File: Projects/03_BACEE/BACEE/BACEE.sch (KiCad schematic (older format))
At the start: 12 parts

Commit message: Project 3: Arrange symbols
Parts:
- added U?: 24LC1025, symbol Memory_EEPROM:24LC1025
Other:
- moved on the sheet: BT?, C?, D?, R?, U?, Y?
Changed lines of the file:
@@
 L Device:Battery BT?
 U 1 1 61D22E5D
-P 5250 2650
-F 0 "BT?" H 5358 2696 50  0000 L CNN
-F 1 "Battery" H 5358 2605 50  0000 L CNN
-F 2 "" V 5250 2710 50  0001 C CNN
-F 3 "~" V 5250 2710 50  0001 C CNN
-	1    5250 2650
+P 9250 2100
+F 0 "BT?" H 9358 2146 50  0000 L CNN
+F 1 "Battery" H 9358 2055 50  0000 L CNN
+F 2 "" V 9250 2160 50  0001 C CNN
+F 3 "~" V 9250 2160 50  0001 C CNN
+	1    9250 2100
 	1    0    0    -1
 $EndComp
@@
 L Device:LED D?
 U 1 1 61D23F53
-P 5250 3200
-F 0 "D?" H 5243 3417 50  0000 C CNN
-F 1 "LED" H 5243 3326 50  0000 C CNN
-F 2 "" H 5250 3200 50  0001 C CNN
-F 3 "~" H 5250 3200 50  0001 C CNN
-	1    5250 3200
+P 5600 3150
+F 0 "D?" H 5593 3367 50  0000 C CNN
+F 1 "LED" H 5593 3276 50  0000 C CNN
+F 2 "" H 5600 3150 50  0001 C CNN
+F 3 "~" H 5600 3150 50  0001 C CNN
+	1    5600 3150
 	1    0    0    -1
 $EndComp
@@
 L Device:C C?
 U 1 1 61D244B0
-P 6100 2350
-F 0 "C?" H 6215 2396 50  0000 L CNN
-F 1 "C" H 6215 2305 50  0000 L CNN
-F 2 "" H 6138 2200 50  0001 C CNN
-F 3 "~" H 6100 2350 50  0001 C CNN
-	1    6100 2350
+P 5050 2050
+F 0 "C?" H 5165 2096 50  0000 L CNN
+F 1 "C" H 5165 2005 50  0000 L CNN
+F 2 "" H 5088 1900 50  0001 C CNN
+F 3 "~" H 5050 2050 50  0001 C CNN
+	1    5050 2050
 	1    0    0    -1
 $EndComp
@@
 L Device:C C?
 U 1 1 61D24B04
-P 6100 2900
-F 0 "C?" H 6215 2946 50  0000 L CNN
-F 1 "C" H 6215 2855 50  0000 L CNN
-F 2 "" H 6138 2750 50  0001 C CNN
-F 3 "~" H 6100 2900 50  0001 C CNN
-	1    6100 2900
+P 5050 2600
+F 0 "C?" H 5165 2646 50  0000 L CNN
+F 1 "C" H 5165 2555 50  0000 L CNN
+F 2 "" H 5088 2450 50  0001 C CNN
+F 3 "~" H 5050 2600 50  0001 C CNN
+	1    5050 2600
 	1    0    0    -1
 $EndComp
@@
 L Device:CP C?
 U 1 1 61D25462
-P 6100 3450
-F 0 "C?" H 6218 3496 50  0000 L CNN
-F 1 "CP" H 6218 3405 50  0000 L CNN
-F 2 "" H 6138 3300 50  0001 C CNN
-F 3 "~" H 6100 3450 50  0001 C CNN
-	1    6100 3450
+P 9950 2750
+F 0 "C?" H 10068 2796 50  0000 L CNN
+F 1 "CP" H 10068 2705 50  0000 L CNN
+F 2 "" H 9988 2600 50  0001 C CNN
+F 3 "~" H 9950 2750 50  0001 C CNN
+	1    9950 2750
 	1    0    0    -1
 $EndComp
@@
 L Device:R R?
 U 1 1 61D25BF7
-P 6900 2350
-F 0 "R?" H 6970 2396 50  0000 L CNN
-F 1 "R" H 6970 2305 50  0000 L CNN
-F 2 "" V 6830 2350 50  0001 C CNN
-F 3 "~" H 6900 2350 50  0001 C CNN
-	1    6900 2350
+P 4950 3300
+F 0 "R?" H 5020 3346 50  0000 L CNN
+F 1 "R" H 5020 3255 50  0000 L CNN
+F 2 "" V 4880 3300 50  0001 C CNN
+F 3 "~" H 4950 3300 50  0001 C CNN
+	1    4950 3300
 	1    0    0    -1
 $EndComp
@@
 L Device:R R?
 U 1 1 61D26130
-P 6900 2900
-F 0 "R?" H 6970 2946 50  0000 L CNN
-F 1 "R" H 6970 2855 50  0000 L CNN
-F 2 "" V 6830 2900 50  0001 C CNN
-F 3 "~" H 6900 2900 50  0001 C CNN
-	1    6900 2900
+P 4950 3850
+F 0 "R?" H 5020 3896 50  0000 L CNN
+F 1 "R" H 5020 3805 50  0000 L CNN
+F 2 "" V 4880 3850 50  0001 C CNN
+F 3 "~" H 4950 3850 50  0001 C CNN
+	1    4950 3850
 	1    0    0    -1
 $EndComp
@@
 L Memory_EEPROM:24LC1025 U?
 U 1 1 61D26D32
-P 8000 2600
-F 0 "U?" H 8000 3081 50  0000 C CNN
-F 1 "24LC1025" H 8000 2990 50  0000 C CNN
-F 2 "" H 8000 2600 50  0001 C CNN
-F 3 "http://ww1.microchip.com/downloads/en/DeviceDoc/21941B.pdf" H 8000 2600 50  0001 C CNN
-	1    8000 2600
+P 3000 5100
+F 0 "U?" H 3000 5581 50  0000 C CNN
+F 1 "24LC1025" H 3000 5490 50  0000 C CNN
+F 2 "" H 3000 5100 50  0001 C CNN
+F 3 "http://ww1.microchip.com/downloads/en/DeviceDoc/21941B.pdf" H 3000 5100 50  0001 C CNN
+	1    3000 5100
 	1    0    0    -1
 $EndComp
 $Sheet
-S 7600 3250 1650 2150
+S 5100 5900 1000 1100
 U 61D27AD2
 F0 "Connectors" 50
@@
 L MCU_Microchip_ATmega:ATmega328P-AU U?
 U 1 1 61D2E20A
-P 4150 3750
-F 0 "U?" H 4150 2161 50  0000 C CNN
-F 1 "ATmega328P-AU" H 4150 2070 50  0000 C CNN
-F 2 "Package_QFP:TQFP-32_7x7mm_P0.8mm" H 4150 3750 50  0001 C CIN
-F 3 "http://ww1.microchip.com/downloads/en/DeviceDoc/ATmega328_P%20AVR%20MCU%20with%20picoPower%20Technology%20Data%20Sheet%2040001984A.pdf" H 4150 3750 50  0001 C CNN
-	1    4150 3750
+P 7000 3500
+F 0 "U?" H 7000 1911 50  0000 C CNN
+F 1 "ATmega328P-AU" H 7000 1820 50  0000 C CNN
+F 2 "Package_QFP:TQFP-32_7x7mm_P0.8mm" H 7000 3500 50  0001 C CIN
+F 3 "http://ww1.microchip.com/downloads/en/DeviceDoc/ATmega328_P%20AVR%20MCU%20with%20picoPower%20Technology%20Data%20Sheet%2040001984A.pdf" H 7000 3500 50  0001 C CNN
+	1    7000 3500
 	1    0    0    -1
 $EndComp
@@
 L Project3:DS1337_MLv1 U?
 U 1 1 61D31649
-P 6200 4800
-F 0 "U?" H 6200 5031 50  0000 C CNN
-F 1 "DS1337_MLv1" H 6200 4940 50  0000 C CNN
-F 2 "" H 6500 4800 50  0001 C CNN
-F 3 "https://datasheets.maximintegrated.com/en/ds/DS1337-DS1337C.pdf" H 6500 4800 50  0001 C CNN
-	1    6200 4800
+P 2950 2150
+F 0 "U?" H 2950 2381 50  0000 C CNN
+F 1 "DS1337_MLv1" H 2950 2290 50  0000 C CNN
+F 2 "" H 3250 2150 50  0001 C CNN
+F 3 "https://datasheets.maximintegrated.com/en/ds/DS1337-DS1337C.pdf" H 3250 2150 50  0001 C CNN
+	1    2950 2150
 	1    0    0    -1
 $EndComp
@@
 L Device:Crystal Y?
 U 1 1 61D3267A
-P 2950 2550
-F 0 "Y?" H 2950 2818 50  0000 C CNN
-F 1 "Crystal" H 2950 2727 50  0000 C CNN
-F 2 "" H 2950 2550 50  0001 C CNN
-F 3 "~" H 2950 2550 50  0001 C CNN
-	1    2950 2550
-	1    0    0    -1
+P 5800 2300
+F 0 "Y?" V 5754 2431 50  0000 L CNN
+F 1 "Crystal" V 5845 2431 50  0000 L CNN
+F 2 "" H 5800 2300 50  0001 C CNN
+F 3 "~" H 5800 2300 50  0001 C CNN
+	1    5800 2300
+	0    1    1    0
 $EndComp
 $Comp
 L Device:Crystal Y?
 U 1 1 61D331D7
-P 2950 3350
-F 0 "Y?" H 2950 3618 50  0000 C CNN
-F 1 "Crystal" H 2950 3527 50  0000 C CNN
-F 2 "" H 2950 3350 50  0001 C CNN
-F 3 "~" H 2950 3350 50  0001 C CNN
-	1    2950 3350
+P 1900 2450
+F 0 "Y?" H 1900 2718 50  0000 C CNN
+F 1 "Crystal" H 1900 2627 50  0000 C CNN
+F 2 "" H 1900 2450 50  0001 C CNN
+F 3 "~" H 1900 2450 50  0001 C CNN
+	1    1900 2450
 	1    0    0    -1
 $EndComp
+$Comp
+L Memory_EEPROM:24LC1025 U?
+U 1 1 61D3DE19
+P 3000 4100
+F 0 "U?" H 3000 4581 50  0000 C CNN
+F 1 "24LC1025" H 3000 4490 50  0000 C CNN
+F 2 "" H 3000 4100 50  0001 C CNN
+F 3 "http://ww1.microchip.com/downloads/en/DeviceDoc/21941B.pdf" H 3000 4100 50  0001 C CNN
+	1    3000 4100
+	1    0    0    -1
+$EndComp
+$Comp
+L power:GND #PWR?
+U 1 1 61D47A07
+P 9250 3300
+F 0 "#PWR?" H 9250 3050 50  0001 C CNN
+F 1 "GND" H 9255 3127 50  0000 C CNN
+F 2 "" H 9250 3300 50  0001 C CNN
+F 3 "" H 9250 3300 50  0001 C CNN
+	1    9250 3300
+	1    0    0    -1
+$EndComp

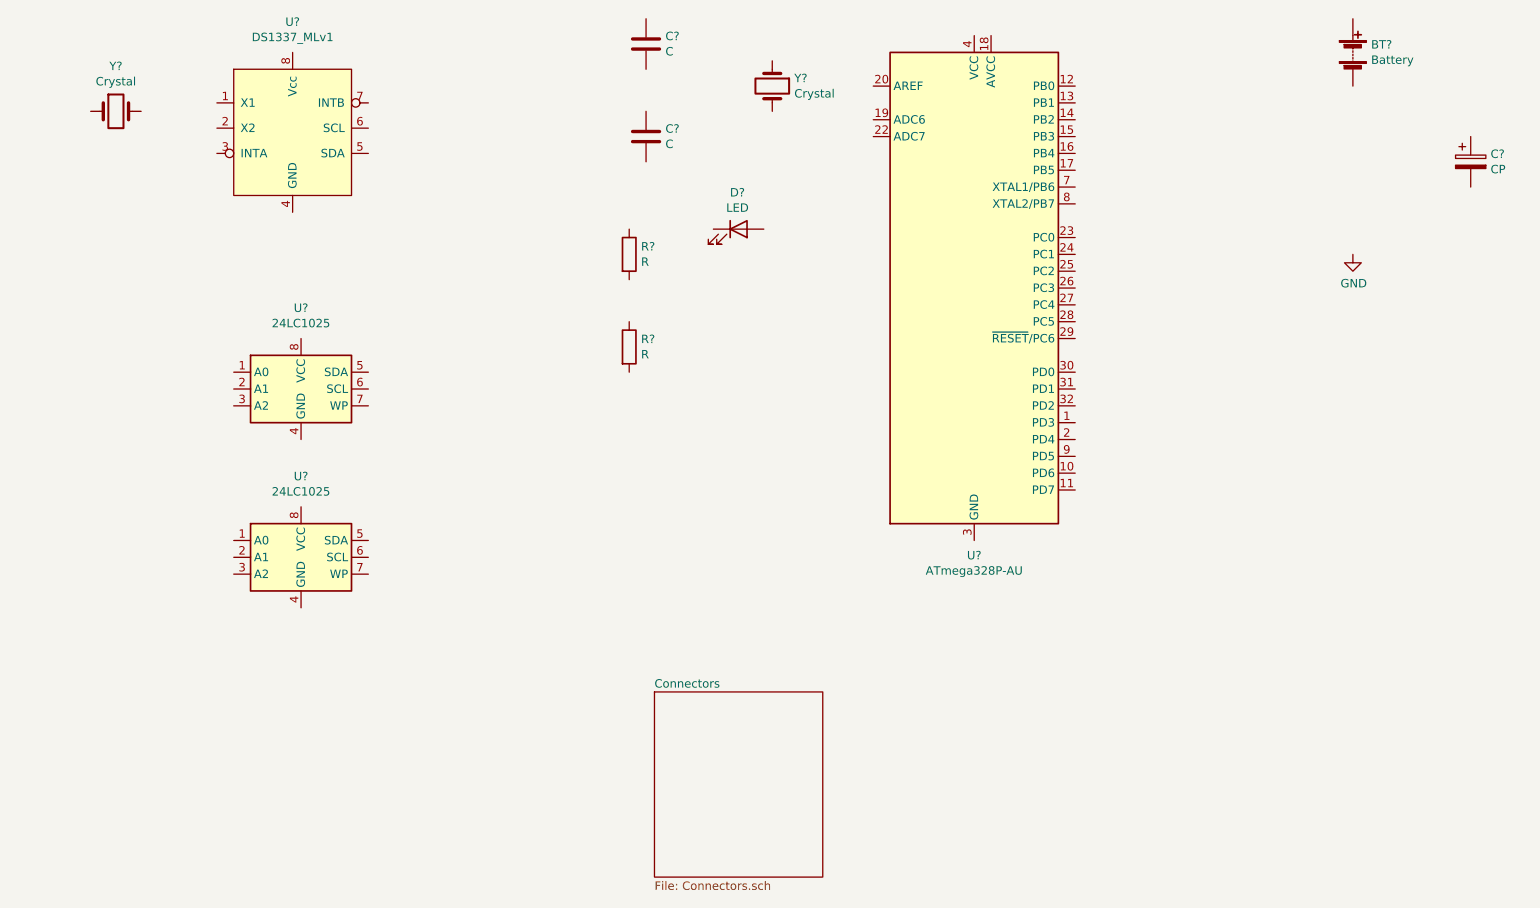
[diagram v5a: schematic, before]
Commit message: Project 3: Annotate schematic
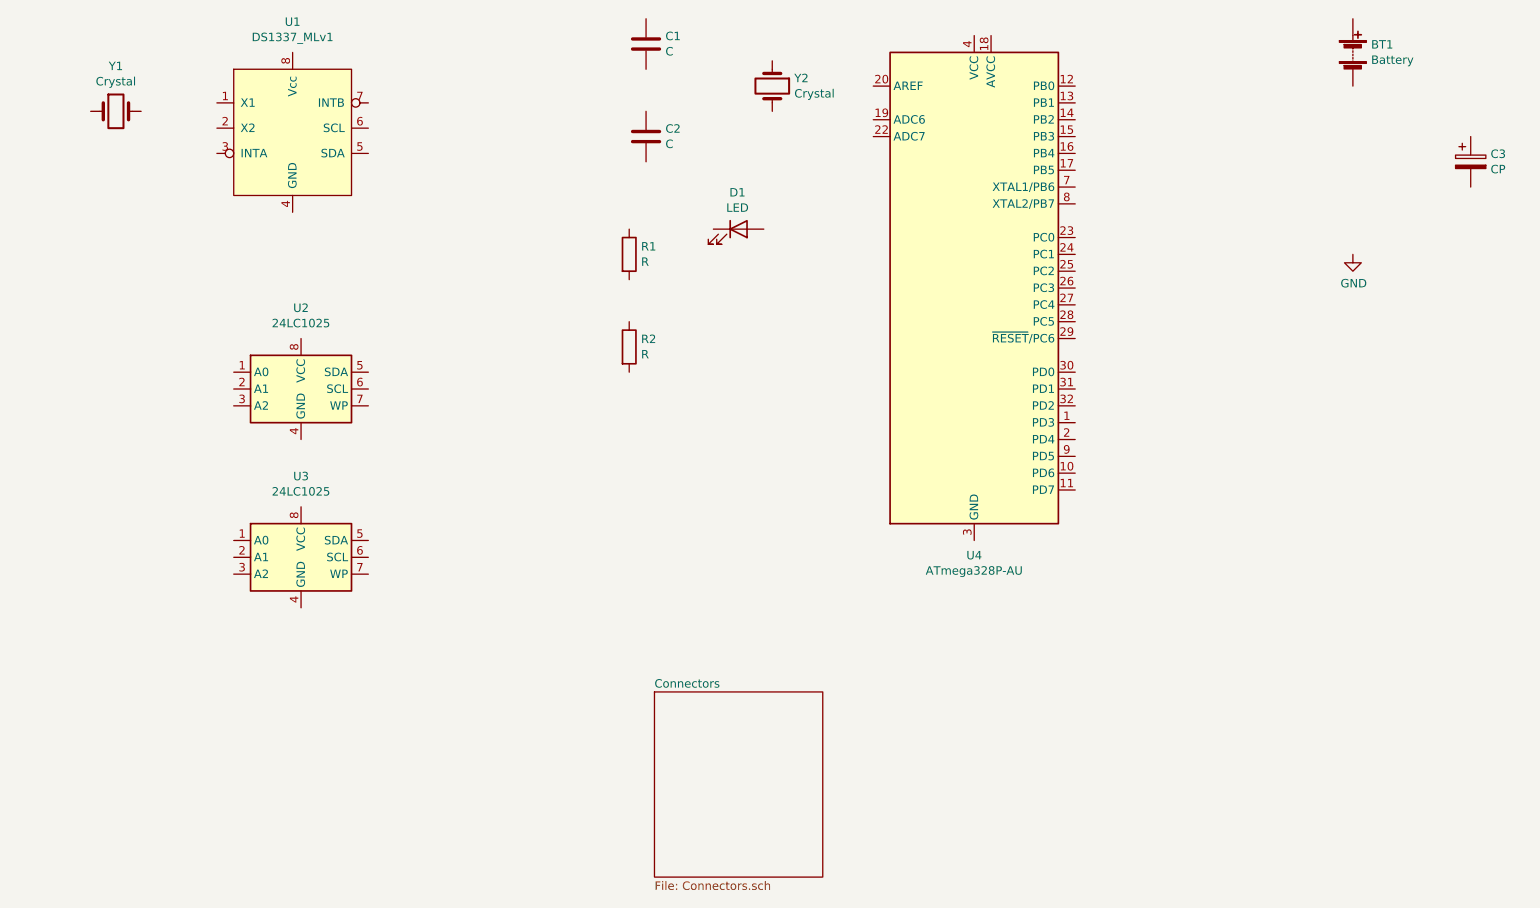
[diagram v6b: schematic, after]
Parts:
- gave numbers to parts that had none: 13
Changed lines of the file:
@@
 $EndDescr
 $Comp
-L Device:Battery BT?
+L Device:Battery BT1
 U 1 1 61D22E5D
 P 9250 2100
-F 0 "BT?" H 9358 2146 50  0000 L CNN
+F 0 "BT1" H 9358 2146 50  0000 L CNN
 F 1 "Battery" H 9358 2055 50  0000 L CNN
 F 2 "" V 9250 2160 50  0001 C CNN
@@
 $EndComp
 $Comp
-L Device:LED D?
+L Device:LED D1
 U 1 1 61D23F53
 P 5600 3150
-F 0 "D?" H 5593 3367 50  0000 C CNN
+F 0 "D1" H 5593 3367 50  0000 C CNN
 F 1 "LED" H 5593 3276 50  0000 C CNN
 F 2 "" H 5600 3150 50  0001 C CNN
@@
 $EndComp
 $Comp
-L Device:C C?
+L Device:C C1
 U 1 1 61D244B0
 P 5050 2050
-F 0 "C?" H 5165 2096 50  0000 L CNN
+F 0 "C1" H 5165 2096 50  0000 L CNN
 F 1 "C" H 5165 2005 50  0000 L CNN
 F 2 "" H 5088 1900 50  0001 C CNN
@@
 $EndComp
 $Comp
-L Device:C C?
+L Device:C C2
 U 1 1 61D24B04
 P 5050 2600
-F 0 "C?" H 5165 2646 50  0000 L CNN
+F 0 "C2" H 5165 2646 50  0000 L CNN
 F 1 "C" H 5165 2555 50  0000 L CNN
 F 2 "" H 5088 2450 50  0001 C CNN
@@
 $EndComp
 $Comp
-L Device:CP C?
+L Device:CP C3
 U 1 1 61D25462
 P 9950 2750
-F 0 "C?" H 10068 2796 50  0000 L CNN
+F 0 "C3" H 10068 2796 50  0000 L CNN
 F 1 "CP" H 10068 2705 50  0000 L CNN
 F 2 "" H 9988 2600 50  0001 C CNN
@@
 $EndComp
 $Comp
-L Device:R R?
+L Device:R R1
 U 1 1 61D25BF7
 P 4950 3300
-F 0 "R?" H 5020 3346 50  0000 L CNN
+F 0 "R1" H 5020 3346 50  0000 L CNN
 F 1 "R" H 5020 3255 50  0000 L CNN
 F 2 "" V 4880 3300 50  0001 C CNN
@@
 $EndComp
 $Comp
-L Device:R R?
+L Device:R R2
 U 1 1 61D26130
 P 4950 3850
-F 0 "R?" H 5020 3896 50  0000 L CNN
+F 0 "R2" H 5020 3896 50  0000 L CNN
 F 1 "R" H 5020 3805 50  0000 L CNN
 F 2 "" V 4880 3850 50  0001 C CNN
@@
 $EndComp
 $Comp
-L Memory_EEPROM:24LC1025 U?
+L Memory_EEPROM:24LC1025 U3
 U 1 1 61D26D32
 P 3000 5100
-F 0 "U?" H 3000 5581 50  0000 C CNN
+F 0 "U3" H 3000 5581 50  0000 C CNN
 F 1 "24LC1025" H 3000 5490 50  0000 C CNN
 F 2 "" H 3000 5100 50  0001 C CNN
@@
 $EndSheet
 $Comp
-L MCU_Microchip_ATmega:ATmega328P-AU U?
+L MCU_Microchip_ATmega:ATmega328P-AU U4
 U 1 1 61D2E20A
 P 7000 3500
-F 0 "U?" H 7000 1911 50  0000 C CNN
+F 0 "U4" H 7000 1911 50  0000 C CNN
 F 1 "ATmega328P-AU" H 7000 1820 50  0000 C CNN
 F 2 "Package_QFP:TQFP-32_7x7mm_P0.8mm" H 7000 3500 50  0001 C CIN
@@
 $EndComp
 $Comp
-L Project3:DS1337_MLv1 U?
+L Project3:DS1337_MLv1 U1
 U 1 1 61D31649
 P 2950 2150
-F 0 "U?" H 2950 2381 50  0000 C CNN
+F 0 "U1" H 2950 2381 50  0000 C CNN
 F 1 "DS1337_MLv1" H 2950 2290 50  0000 C CNN
 F 2 "" H 3250 2150 50  0001 C CNN
@@
 $EndComp
 $Comp
-L Device:Crystal Y?
+L Device:Crystal Y2
 U 1 1 61D3267A
 P 5800 2300
-F 0 "Y?" V 5754 2431 50  0000 L CNN
+F 0 "Y2" V 5754 2431 50  0000 L CNN
 F 1 "Crystal" V 5845 2431 50  0000 L CNN
 F 2 "" H 5800 2300 50  0001 C CNN
@@
 $EndComp
 $Comp
-L Device:Crystal Y?
+L Device:Crystal Y1
 U 1 1 61D331D7
 P 1900 2450
-F 0 "Y?" H 1900 2718 50  0000 C CNN
+F 0 "Y1" H 1900 2718 50  0000 C CNN
 F 1 "Crystal" H 1900 2627 50  0000 C CNN
 F 2 "" H 1900 2450 50  0001 C CNN
@@
 $EndComp
 $Comp
-L Memory_EEPROM:24LC1025 U?
+L Memory_EEPROM:24LC1025 U2
 U 1 1 61D3DE19
 P 3000 4100
-F 0 "U?" H 3000 4581 50  0000 C CNN
+F 0 "U2" H 3000 4581 50  0000 C CNN
 F 1 "24LC1025" H 3000 4490 50  0000 C CNN
 F 2 "" H 3000 4100 50  0001 C CNN
@@
 $EndComp
 $Comp
-L power:GND #PWR?
+L power:GND #PWR01
 U 1 1 61D47A07
 P 9250 3300
-F 0 "#PWR?" H 9250 3050 50  0001 C CNN
+F 0 "#PWR01" H 9250 3050 50  0001 C CNN
 F 1 "GND" H 9255 3127 50  0000 C CNN
 F 2 "" H 9250 3300 50  0001 C CNN

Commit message: Project 3: Associate footprints
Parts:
- BT1: footprint (none) -> Connector_PinHeader_2.54mm:PinHeader_1x02_P2.54mm_Vertical
- C1, C2, C3: footprint (none) -> Diode_SMD:D_0805_2012Metric_Pad1.15x1.40mm_HandSolder
- D1: footprint (none) -> LED_SMD:LED_0805_2012Metric_Pad1.15x1.40mm_HandSolder
- R1, R2: footprint (none) -> Resistor_SMD:R_0805_2012Metric_Pad1.20x1.40mm_HandSolder
- U1: footprint (none) -> Package_SO:SO-8_5.3x6.2mm_P1.27mm
- U2, U3: footprint (none) -> Package_SO:SOIJ-8_5.3x5.3mm_P1.27mm
- Y1: footprint (none) -> Crystal:Crystal_SMD_MicroCrystal_CC7V-T1A-2Pin_3.2x1.5mm
- Y2: footprint (none) -> Crystal:Crystal_SMD_5032-2Pin_5.0x3.2mm_HandSoldering
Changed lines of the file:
@@
 F 0 "BT1" H 9358 2146 50  0000 L CNN
 F 1 "Battery" H 9358 2055 50  0000 L CNN
-F 2 "" V 9250 2160 50  0001 C CNN
+F 2 "Connector_PinHeader_2.54mm:PinHeader_1x02_P2.54mm_Vertical" V 9250 2160 50  0001 C CNN
 F 3 "~" V 9250 2160 50  0001 C CNN
 	1    9250 2100
@@
 F 0 "D1" H 5593 3367 50  0000 C CNN
 F 1 "LED" H 5593 3276 50  0000 C CNN
-F 2 "" H 5600 3150 50  0001 C CNN
+F 2 "LED_SMD:LED_0805_2012Metric_Pad1.15x1.40mm_HandSolder" H 5600 3150 50  0001 C CNN
 F 3 "~" H 5600 3150 50  0001 C CNN
 	1    5600 3150
@@
 F 0 "C1" H 5165 2096 50  0000 L CNN
 F 1 "C" H 5165 2005 50  0000 L CNN
-F 2 "" H 5088 1900 50  0001 C CNN
+F 2 "Diode_SMD:D_0805_2012Metric_Pad1.15x1.40mm_HandSolder" H 5088 1900 50  0001 C CNN
 F 3 "~" H 5050 2050 50  0001 C CNN
 	1    5050 2050
@@
 F 0 "C2" H 5165 2646 50  0000 L CNN
 F 1 "C" H 5165 2555 50  0000 L CNN
-F 2 "" H 5088 2450 50  0001 C CNN
+F 2 "Diode_SMD:D_0805_2012Metric_Pad1.15x1.40mm_HandSolder" H 5088 2450 50  0001 C CNN
 F 3 "~" H 5050 2600 50  0001 C CNN
 	1    5050 2600
@@
 F 0 "C3" H 10068 2796 50  0000 L CNN
 F 1 "CP" H 10068 2705 50  0000 L CNN
-F 2 "" H 9988 2600 50  0001 C CNN
+F 2 "Diode_SMD:D_0805_2012Metric_Pad1.15x1.40mm_HandSolder" H 9988 2600 50  0001 C CNN
 F 3 "~" H 9950 2750 50  0001 C CNN
 	1    9950 2750
@@
 F 0 "R1" H 5020 3346 50  0000 L CNN
 F 1 "R" H 5020 3255 50  0000 L CNN
-F 2 "" V 4880 3300 50  0001 C CNN
+F 2 "Resistor_SMD:R_0805_2012Metric_Pad1.20x1.40mm_HandSolder" V 4880 3300 50  0001 C CNN
 F 3 "~" H 4950 3300 50  0001 C CNN
 	1    4950 3300
@@
 F 0 "R2" H 5020 3896 50  0000 L CNN
 F 1 "R" H 5020 3805 50  0000 L CNN
-F 2 "" V 4880 3850 50  0001 C CNN
+F 2 "Resistor_SMD:R_0805_2012Metric_Pad1.20x1.40mm_HandSolder" V 4880 3850 50  0001 C CNN
 F 3 "~" H 4950 3850 50  0001 C CNN
 	1    4950 3850
@@
 F 0 "U3" H 3000 5581 50  0000 C CNN
 F 1 "24LC1025" H 3000 5490 50  0000 C CNN
-F 2 "" H 3000 5100 50  0001 C CNN
+F 2 "Package_SO:SOIJ-8_5.3x5.3mm_P1.27mm" H 3000 5100 50  0001 C CNN
 F 3 "http://ww1.microchip.com/downloads/en/DeviceDoc/21941B.pdf" H 3000 5100 50  0001 C CNN
 	1    3000 5100
@@
 F 0 "U1" H 2950 2381 50  0000 C CNN
 F 1 "DS1337_MLv1" H 2950 2290 50  0000 C CNN
-F 2 "" H 3250 2150 50  0001 C CNN
+F 2 "Package_SO:SO-8_5.3x6.2mm_P1.27mm" H 3250 2150 50  0001 C CNN
 F 3 "https://datasheets.maximintegrated.com/en/ds/DS1337-DS1337C.pdf" H 3250 2150 50  0001 C CNN
 	1    2950 2150
@@
 F 0 "Y2" V 5754 2431 50  0000 L CNN
 F 1 "Crystal" V 5845 2431 50  0000 L CNN
-F 2 "" H 5800 2300 50  0001 C CNN
+F 2 "Crystal:Crystal_SMD_5032-2Pin_5.0x3.2mm_HandSoldering" H 5800 2300 50  0001 C CNN
 F 3 "~" H 5800 2300 50  0001 C CNN
 	1    5800 2300
@@
 F 0 "Y1" H 1900 2718 50  0000 C CNN
 F 1 "Crystal" H 1900 2627 50  0000 C CNN
-F 2 "" H 1900 2450 50  0001 C CNN
+F 2 "Crystal:Crystal_SMD_MicroCrystal_CC7V-T1A-2Pin_3.2x1.5mm" H 1900 2450 50  0001 C CNN
 F 3 "~" H 1900 2450 50  0001 C CNN
 	1    1900 2450
@@
 F 0 "U2" H 3000 4581 50  0000 C CNN
 F 1 "24LC1025" H 3000 4490 50  0000 C CNN
-F 2 "" H 3000 4100 50  0001 C CNN
+F 2 "Package_SO:SOIJ-8_5.3x5.3mm_P1.27mm" H 3000 4100 50  0001 C CNN
 F 3 "http://ww1.microchip.com/downloads/en/DeviceDoc/21941B.pdf" H 3000 4100 50  0001 C CNN
 	1    3000 4100

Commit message: Project 3: Complete associations and add component values
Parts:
- BT1: value Battery -> Battery 3V
- C1, C2: value C -> 22pF
- C3: value CP -> 10uF
- R1: value R -> 330Ohm
- R2: value R -> 10kOhm
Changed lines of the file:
@@
 P 9250 2100
 F 0 "BT1" H 9358 2146 50  0000 L CNN
-F 1 "Battery" H 9358 2055 50  0000 L CNN
+F 1 "Battery 3V" H 9358 2055 50  0000 L CNN
 F 2 "Connector_PinHeader_2.54mm:PinHeader_1x02_P2.54mm_Vertical" V 9250 2160 50  0001 C CNN
 F 3 "~" V 9250 2160 50  0001 C CNN
@@
 P 5050 2050
 F 0 "C1" H 5165 2096 50  0000 L CNN
-F 1 "C" H 5165 2005 50  0000 L CNN
+F 1 "22pF" H 5165 2005 50  0000 L CNN
 F 2 "Diode_SMD:D_0805_2012Metric_Pad1.15x1.40mm_HandSolder" H 5088 1900 50  0001 C CNN
 F 3 "~" H 5050 2050 50  0001 C CNN
@@
 P 5050 2600
 F 0 "C2" H 5165 2646 50  0000 L CNN
-F 1 "C" H 5165 2555 50  0000 L CNN
+F 1 "22pF" H 5165 2555 50  0000 L CNN
 F 2 "Diode_SMD:D_0805_2012Metric_Pad1.15x1.40mm_HandSolder" H 5088 2450 50  0001 C CNN
 F 3 "~" H 5050 2600 50  0001 C CNN
@@
 P 9950 2750
 F 0 "C3" H 10068 2796 50  0000 L CNN
-F 1 "CP" H 10068 2705 50  0000 L CNN
+F 1 "10uF" H 10068 2705 50  0000 L CNN
 F 2 "Diode_SMD:D_0805_2012Metric_Pad1.15x1.40mm_HandSolder" H 9988 2600 50  0001 C CNN
 F 3 "~" H 9950 2750 50  0001 C CNN
@@
 P 4950 3300
 F 0 "R1" H 5020 3346 50  0000 L CNN
-F 1 "R" H 5020 3255 50  0000 L CNN
+F 1 "330Ohm" H 5020 3255 50  0000 L CNN
 F 2 "Resistor_SMD:R_0805_2012Metric_Pad1.20x1.40mm_HandSolder" V 4880 3300 50  0001 C CNN
 F 3 "~" H 4950 3300 50  0001 C CNN
@@
 P 4950 3850
 F 0 "R2" H 5020 3896 50  0000 L CNN
-F 1 "R" H 5020 3805 50  0000 L CNN
+F 1 "10kOhm" H 5020 3805 50  0000 L CNN
 F 2 "Resistor_SMD:R_0805_2012Metric_Pad1.20x1.40mm_HandSolder" V 4880 3850 50  0001 C CNN
 F 3 "~" H 4950 3850 50  0001 C CNN
